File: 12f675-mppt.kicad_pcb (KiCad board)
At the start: 2 copper layers, 97.6 x 77.1 mm, 43 parts, among them IC1 PIC12F629-I/P, J1 S+, J2 S-, J3 O+, J4 O-, Q1 BUK9511-55A127, Q2 BUK9511-55A127, Q3 2N2222A, Q4 2N2222A, Q5 2N2907A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

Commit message: update PCB.
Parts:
- added R11: 10k, Resistors_THT:R_Axial_DIN0309_L9.0mm_D3.2mm_P12.70mm_Horizontal, F.Cu at (93.5, 85.3)
- moved C5 3.36 mm to (102.3, 74.4)
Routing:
- net /BootStrap: track 86.5 -> 97.0 mm
- net Net-(IC1-Pad7): track 8.67 -> 13.7 mm
- net /PV-Current: track 54.1 -> 58.7 mm
- net GNDPWR: track 290.1 -> 291.8 mm
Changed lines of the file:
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@@
     (thickness 1.6)
     (drawings 5)
-    (tracks 210)
+    (tracks 215)
     (zones 0)
-    (modules 43)
+    (modules 44)
     (nets 28)
   )
@@
   )
   (module Capacitors_THT:CP_Radial_D12.5mm_P5.00mm (layer F.Cu)
-    (at 99.02444 75.08748 270)
+    (at 102.32644 74.4474 270)
     (descr "CP, Radial series, Radial, pin pitch=5.00mm, , diameter=12.5mm, Electrolytic Capacitor")
     (tags "CP Radial series Radial pin pitch 5.00mm  diameter 12.5mm Electrolytic Capacitor")
@@
       (net 24 PRI_LO))
   )
+  (module Resistors_THT:R_Axial_DIN0309_L9.0mm_D3.2mm_P12.70mm_Horizontal (layer F.Cu)
+    (at 93.53804 85.33384 90)
+    (descr "Resistor, Axial_DIN0309 series, Axial, Horizontal, pin pitch=12.7mm, 0.5W = 1/2W, length*diameter=9*3.2mm^2, http://cdn-reichelt.de/documents/datenblatt/B400/1_4W%23YAG.pdf")
+    (tags "Resistor Axial_DIN0309 series Axial Horizontal pin pitch 12.7mm 0.5W = 1/2W length 9mm diameter 3.2mm")
+    (fp_text reference R11 (at 0.10668 2.82448 90) (layer F.SilkS)
+      (effects (font (size 1 1) (thickness 0.15)))
+    )
+    (fp_text value 10k (at 6.35 2.66 90) (layer F.Fab)
+      (effects (font (size 1 1) (thickness 0.15)))
+    )
+    (fp_line (start 13.75 -1.95) (end -1.05 -1.95) (layer F.CrtYd) (width 0.05))
+    (fp_line (start 13.75 1.95) (end 13.75 -1.95) (layer F.CrtYd) (width 0.05))
+    (fp_line (start -1.05 1.95) (end 13.75 1.95) (layer F.CrtYd) (width 0.05))
+    (fp_line (start -1.05 -1.95) (end -1.05 1.95) (layer F.CrtYd) (width 0.05))
+    (fp_line (start 11.72 0) (end 10.91 0) (layer F.SilkS) (width 0.12))
+    (fp_line (start 0.98 0) (end 1.79 0) (layer F.SilkS) (width 0.12))
+    (fp_line (start 10.91 -1.66) (end 1.79 -1.66) (layer F.SilkS) (width 0.12))
+    (fp_line (start 10.91 1.66) (end 10.91 -1.66) (layer F.SilkS) (width 0.12))
+    (fp_line (start 1.79 1.66) (end 10.91 1.66) (layer F.SilkS) (width 0.12))
+    (fp_line (start 1.79 -1.66) (end 1.79 1.66) (layer F.SilkS) (width 0.12))
+    (fp_line (start 12.7 0) (end 10.85 0) (layer F.Fab) (width 0.1))
+    (fp_line (start 0 0) (end 1.85 0) (layer F.Fab) (width 0.1))
+    (fp_line (start 10.85 -1.6) (end 1.85 -1.6) (layer F.Fab) (width 0.1))
+    (fp_line (start 10.85 1.6) (end 10.85 -1.6) (layer F.Fab) (width 0.1))
+    (fp_line (start 1.85 1.6) (end 10.85 1.6) (layer F.Fab) (width 0.1))
+    (fp_line (start 1.85 -1.6) (end 1.85 1.6) (layer F.Fab) (width 0.1))
+    (pad 2 thru_hole oval (at 12.7 0 90) (size 1.6 1.6) (drill 0.8) (layers *.Cu *.Mask)
+      (net 13 "Net-(IC1-Pad7)"))
+    (pad 1 thru_hole circle (at 0 0 90) (size 1.6 1.6) (drill 0.8) (layers *.Cu *.Mask)
+      (net 3 /BootStrap))
+    (model ${KISYS3DMOD}/Resistors_THT.3dshapes/R_Axial_DIN0309_L9.0mm_D3.2mm_P12.70mm_Horizontal.wrl
+      (at (xyz 0 0 0))
+      (scale (xyz 0.393701 0.393701 0.393701))
+      (rotate (xyz 0 0 0))
+    )
+  )
   (gr_text "25V 3A" (at 34.83356 57.84088 90) (layer F.SilkS)
     (effects (font (size 1.5 1.5) (thickness 0.3)))
@@
   (segment (start 83.99272 76.89088) (end 83.97748 76.87564) (width 1.5) (layer B.Cu) (net 3))
   (segment (start 88.49868 76.89088) (end 83.99272 76.89088) (width 1.5) (layer B.Cu) (net 3))
+  (segment (start 88.49868 80.29448) (end 93.53804 85.33384) (width 1.5) (layer F.Cu) (net 3))
+  (segment (start 88.49868 76.89088) (end 88.49868 80.29448) (width 1.5) (layer F.Cu) (net 3))
   (segment (start 102.72268 40.606728) (end 102.73284 40.596568) (width 2) (layer B.Cu) (net 4))
   (segment (start 102.72268 41.87952) (end 102.72268 40.606728) (width 2) (layer B.Cu) (net 4))
@@
   (segment (start 76.71308 76.87564) (end 83.91144 69.67728) (width 1.5) (layer F.Cu) (net 10))
   (segment (start 76.35748 76.87564) (end 76.71308 76.87564) (width 1.5) (layer F.Cu) (net 10))
-  (segment (start 96.32444 75.08748) (end 94.16036 72.9234) (width 1.5) (layer F.Cu) (net 10))
-  (segment (start 99.02444 75.08748) (end 96.32444 75.08748) (width 1.5) (layer F.Cu) (net 10))
-  (segment (start 86.61144 69.67728) (end 83.91144 69.67728) (width 1.5) (layer F.Cu) (net 10))
-  (segment (start 89.85756 72.9234) (end 86.61144 69.67728) (width 1.5) (layer F.Cu) (net 10))
-  (segment (start 94.16036 72.9234) (end 89.85756 72.9234) (width 1.5) (layer F.Cu) (net 10))
   (segment (start 76.35748 76.87564) (end 72.46112 76.87564) (width 1.5) (layer F.Cu) (net 10))
   (segment (start 58.2676 91.06916) (end 58.2676 93.28404) (width 1.5) (layer F.Cu) (net 10))
   (segment (start 72.46112 76.87564) (end 58.2676 91.06916) (width 1.5) (layer F.Cu) (net 10))
+  (segment (start 86.61144 69.67728) (end 93.28656 76.3524) (width 1.5) (layer F.Cu) (net 10))
+  (segment (start 83.91144 69.67728) (end 86.61144 69.67728) (width 1.5) (layer F.Cu) (net 10))
+  (segment (start 97.72144 76.3524) (end 93.28656 76.3524) (width 1.5) (layer F.Cu) (net 10))
+  (segment (start 99.62644 74.4474) (end 97.72144 76.3524) (width 1.5) (layer F.Cu) (net 10))
+  (segment (start 102.32644 74.4474) (end 99.62644 74.4474) (width 1.5) (layer F.Cu) (net 10))
   (segment (start 78.99144 64.59728) (end 79.11084 64.71668) (width 1.5) (layer B.Cu) (net 11))
   (segment (start 76.29144 64.59728) (end 78.99144 64.59728) (width 1.5) (layer B.Cu) (net 11))
@@
   (segment (start 86.69528 64.59728) (end 83.91144 64.59728) (width 1.5) (layer B.Cu) (net 13))
   (segment (start 90.86088 68.76288) (end 86.69528 64.59728) (width 1.5) (layer B.Cu) (net 13))
+  (segment (start 93.53804 71.44004) (end 90.86088 68.76288) (width 1.5) (layer B.Cu) (net 13))
+  (segment (start 93.53804 72.63384) (end 93.53804 71.44004) (width 1.5) (layer B.Cu) (net 13))
   (segment (start 50.78388 97.66032) (end 50.78388 104.16032) (width 2) (layer B.Cu) (net 14))
   (segment (start 50.73396 97.6104) (end 50.78388 97.66032) (width 1.5) (layer B.Cu) (net 14))
@@
   (segment (start 88.79332 99.66452) (end 93.5736 99.66452) (width 2) (layer B.Cu) (net 26))
   (segment (start 87.53348 98.40468) (end 88.79332 99.66452) (width 2) (layer B.Cu) (net 26))
-  (segment (start 99.02444 97.11368) (end 99.02444 80.08748) (width 2) (layer B.Cu) (net 26))
-  (segment (start 96.4736 99.66452) (end 99.02444 97.11368) (width 2) (layer B.Cu) (net 26))
-  (segment (start 93.5736 99.66452) (end 96.4736 99.66452) (width 2) (layer B.Cu) (net 26))
+  (segment (start 95.9736 99.66452) (end 98.21672 97.4214) (width 1.5) (layer B.Cu) (net 26))
+  (segment (start 93.5736 99.66452) (end 95.9736 99.66452) (width 1.5) (layer B.Cu) (net 26))
+  (segment (start 98.21672 83.55712) (end 102.32644 79.4474) (width 1.5) (layer B.Cu) (net 26))
+  (segment (start 98.21672 97.4214) (end 98.21672 83.55712) (width 1.5) (layer B.Cu) (net 26))
   (segment (start 40.7162 46.63948) (end 40.78224 46.70552) (width 3) (layer B.Cu) (net 27))
   (segment (start 40.7162 41.60012) (end 40.7162 46.63948) (width 3) (layer B.Cu) (net 27))

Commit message: Change circuit. Exchange GP0(Current Sensing) and GP2(PWM).
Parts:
- R1: value 4.7k -> 10k
- R15: value 10k -> 3.3k
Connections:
- IC1 pad 5: /PV-Current -> Net-(IC1-Pad5)
- IC1 pad 7: Net-(IC1-Pad7) -> /PV-Current
- R11 pad 2: Net-(IC1-Pad7) -> Net-(IC1-Pad5)
- R7 pad 2: Net-(IC1-Pad7) -> Net-(IC1-Pad5)
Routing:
- net Net-(IC1-Pad7): track 13.7 -> 0.00 mm
- net Net-(IC1-Pad5): track 0.00 -> 12.3 mm
- net /PV-Current: track 58.7 -> 69.0 mm

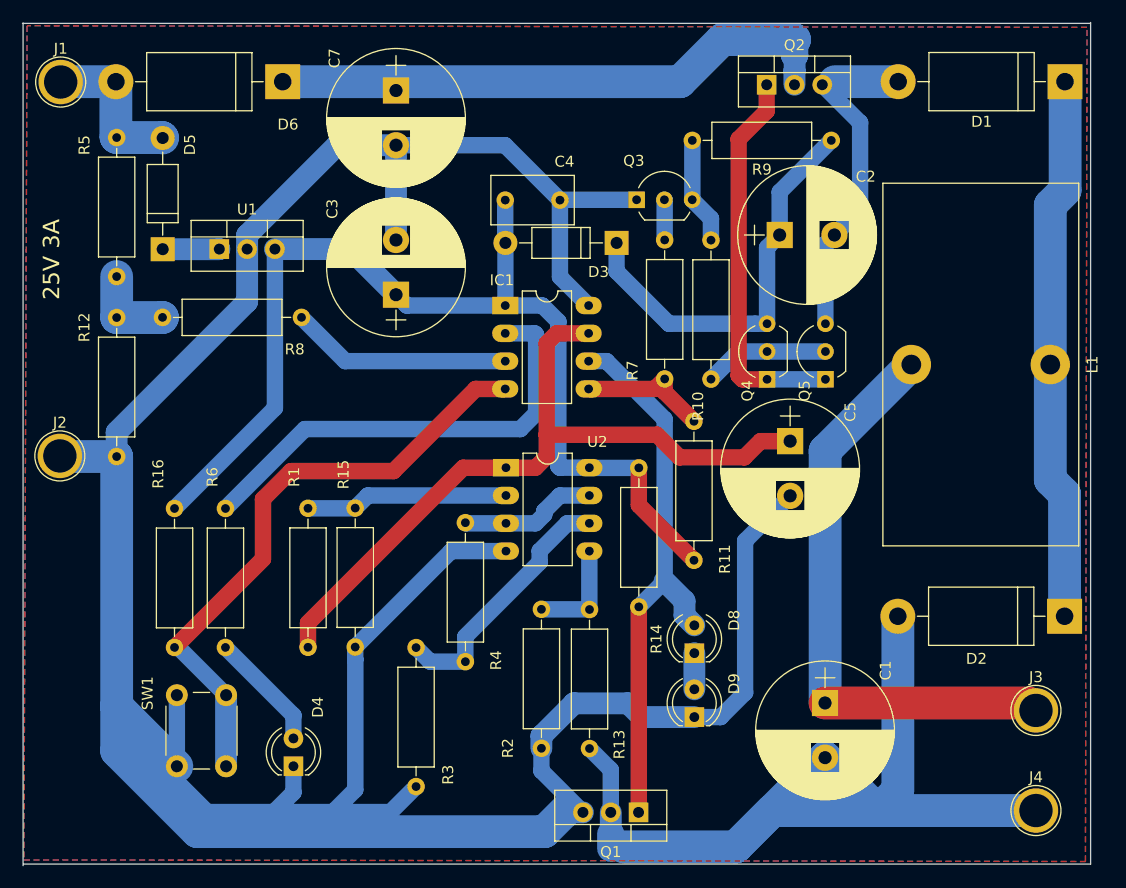
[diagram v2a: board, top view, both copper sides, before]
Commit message: Add FET protection zener diode.
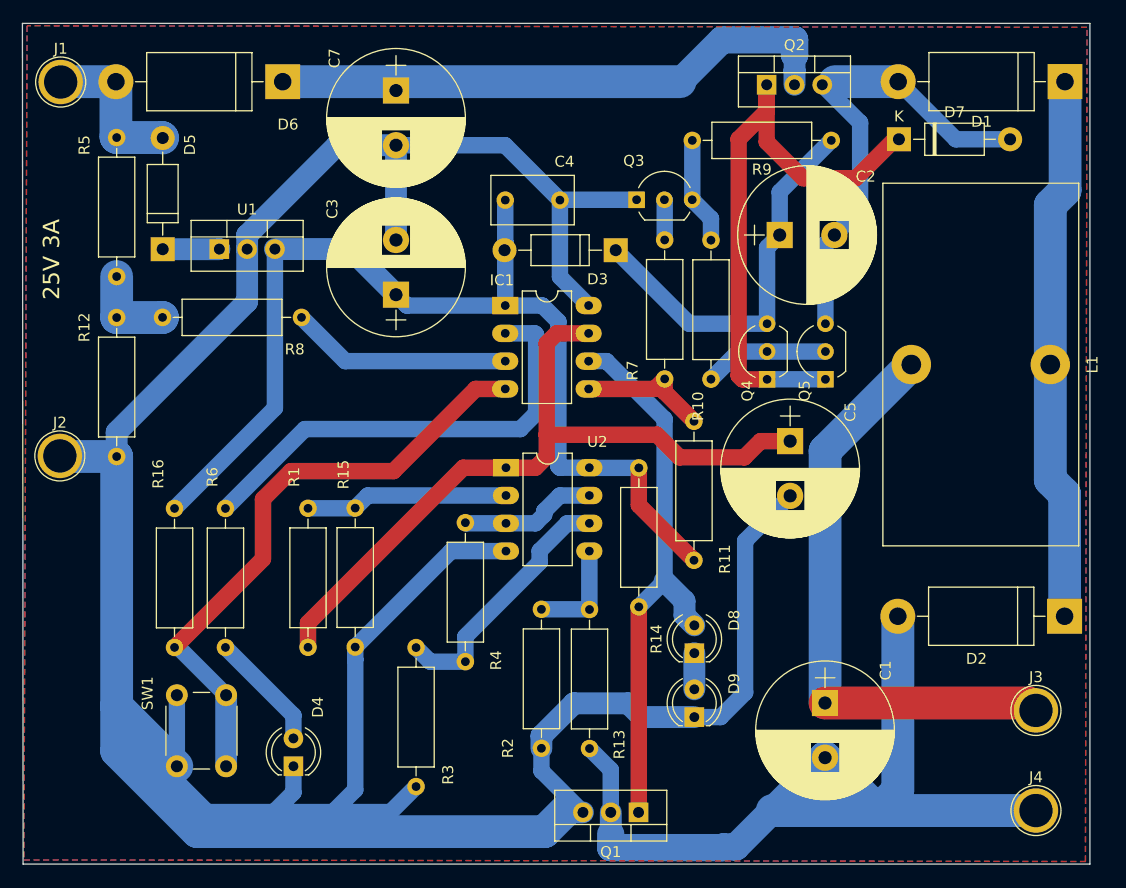
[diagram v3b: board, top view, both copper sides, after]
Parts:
- added D7: 1N4733A 5.1V, Diode_THT:D_DO-41_SOD81_P10.16mm_Horizontal, F.Cu at (112.3, 46.9)
- moved D3 0.67 mm to (86.4, 57.0)
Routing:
- net Net-(D7-Pad1): track 35.7 -> 55.9 mm
- net Net-(C7-Pad1): track 52.6 -> 66.1 mm
- net Net-(C2-Pad2): track 30.4 -> 42.8 mm
- net PRI_LO: track 94.0 -> 88.8 mm
- net Net-(C2-Pad1): track 37.5 -> 35.8 mm
- net /BootStrap: track 97.0 -> 96.3 mm
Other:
- board size 97.6 x 77.1 mm -> 97.6 x 76.8 mm

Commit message: R9 -> 2.2k
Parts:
- R9: value 10k -> 2.2k

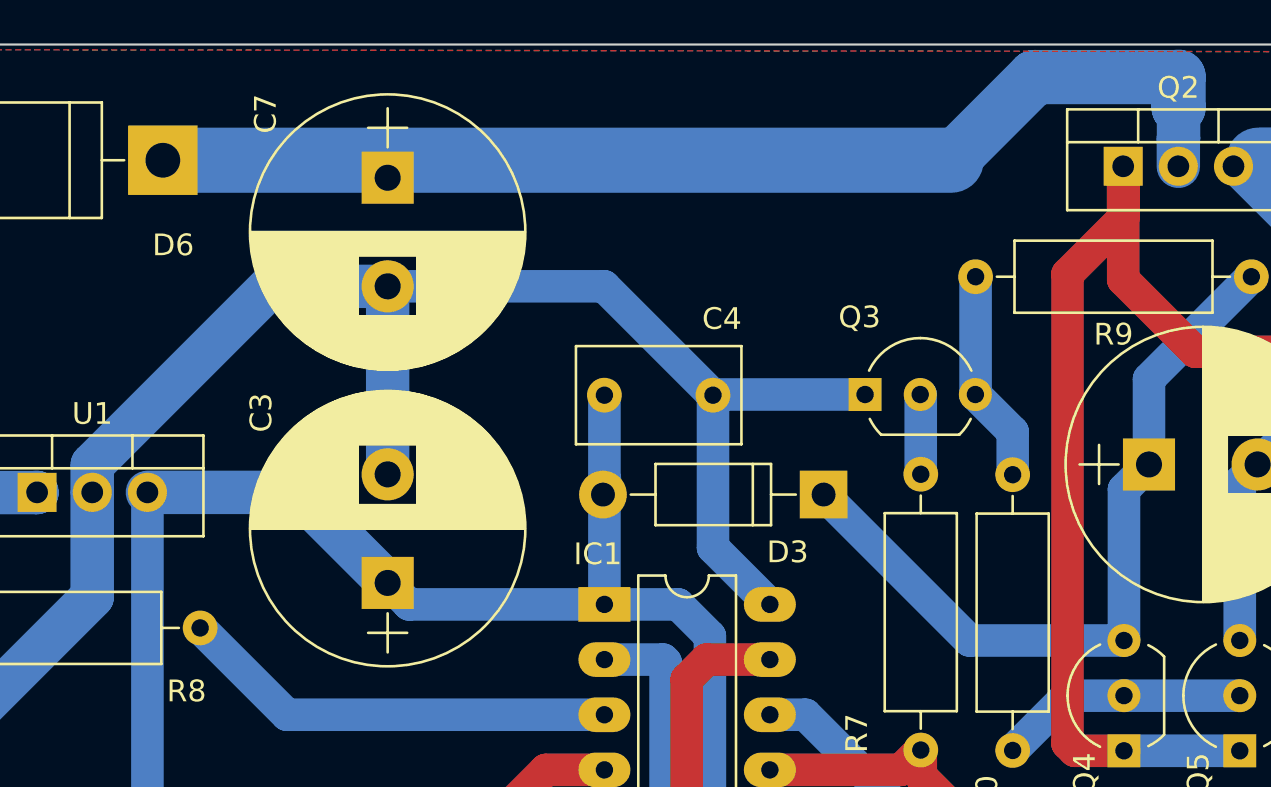
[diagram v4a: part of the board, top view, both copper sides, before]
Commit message: Fix FET Bootstrap problem.
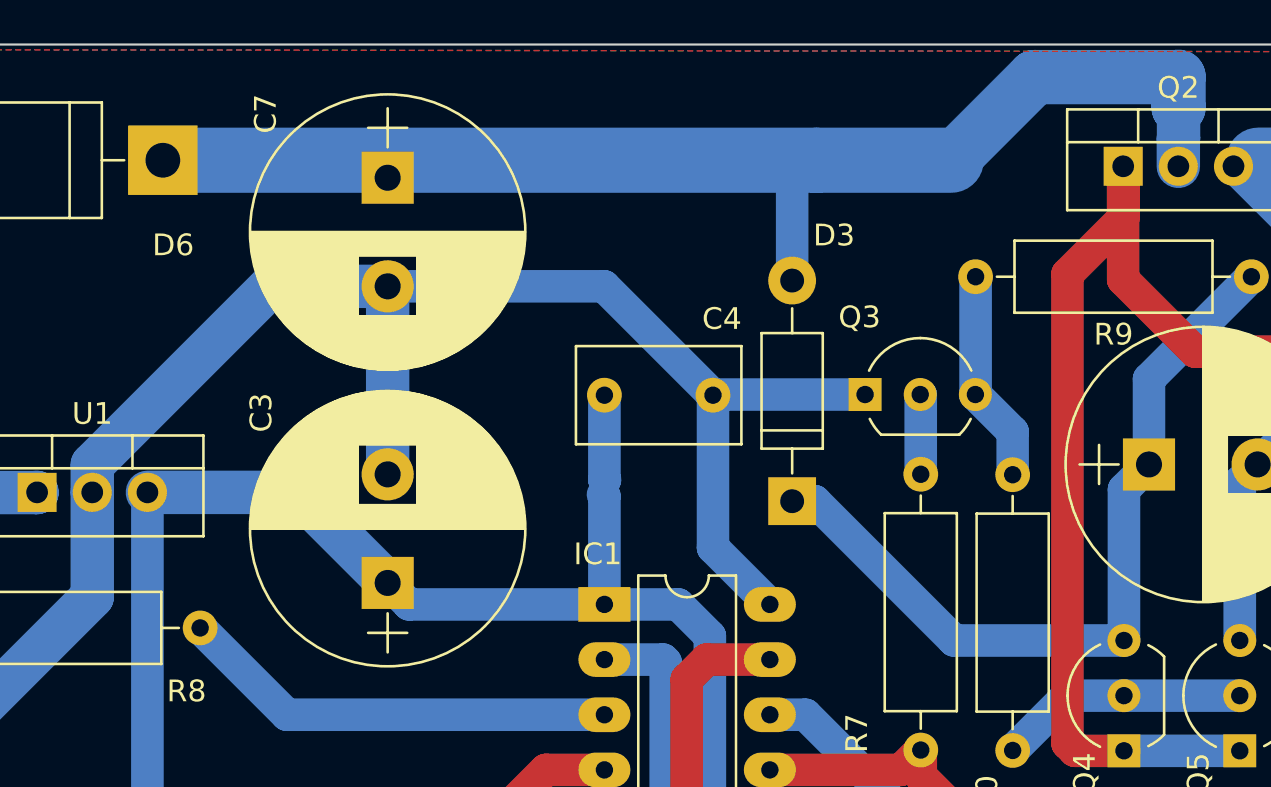
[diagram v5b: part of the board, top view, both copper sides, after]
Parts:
- C2: value 10u 50v -> 4.7u 50v
- moved D3 1.48 mm to (84.9, 57.3), turned to 90 degrees
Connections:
- C2 pad 1: Net-(C2-Pad1) -> /BootStrap
- C3 pad 1: /BootStrap -> Net-(C3-Pad1)
- C4 pad 1: /BootStrap -> Net-(C3-Pad1)
- D3 pad 1: Net-(C2-Pad1) -> /BootStrap
- D3 pad 2: /BootStrap -> Net-(C7-Pad1)
- IC1 pad 1: /BootStrap -> Net-(C3-Pad1)
- Q4 pad 3: Net-(C2-Pad1) -> /BootStrap
- R11 pad 1: /BootStrap -> Net-(C3-Pad1)
- R14 pad 1: /BootStrap -> Net-(C3-Pad1)
- R16 pad 2: /BootStrap -> Net-(C3-Pad1)
- R9 pad 1: Net-(C2-Pad1) -> /BootStrap
- U1 pad 3: /BootStrap -> Net-(C3-Pad1)
- U2 pad 8: /BootStrap -> Net-(C3-Pad1)
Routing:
- net Net-(C3-Pad1): track 0.00 -> 96.3 mm
- net /BootStrap: track 96.3 -> 37.1 mm
- net Net-(C2-Pad1): track 35.8 -> 0.00 mm
- net Net-(C7-Pad1): track 66.1 -> 72.1 mm

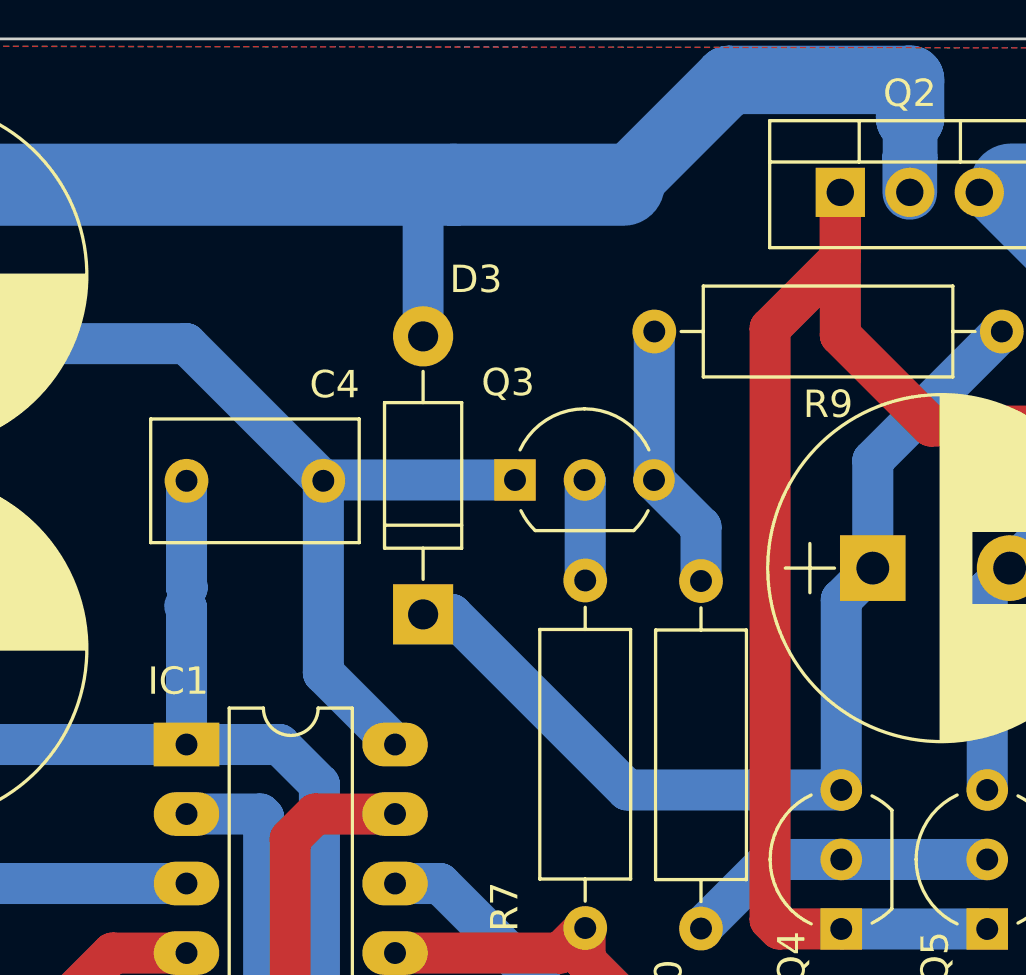
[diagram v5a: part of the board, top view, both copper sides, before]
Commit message: Revert and Change diode.
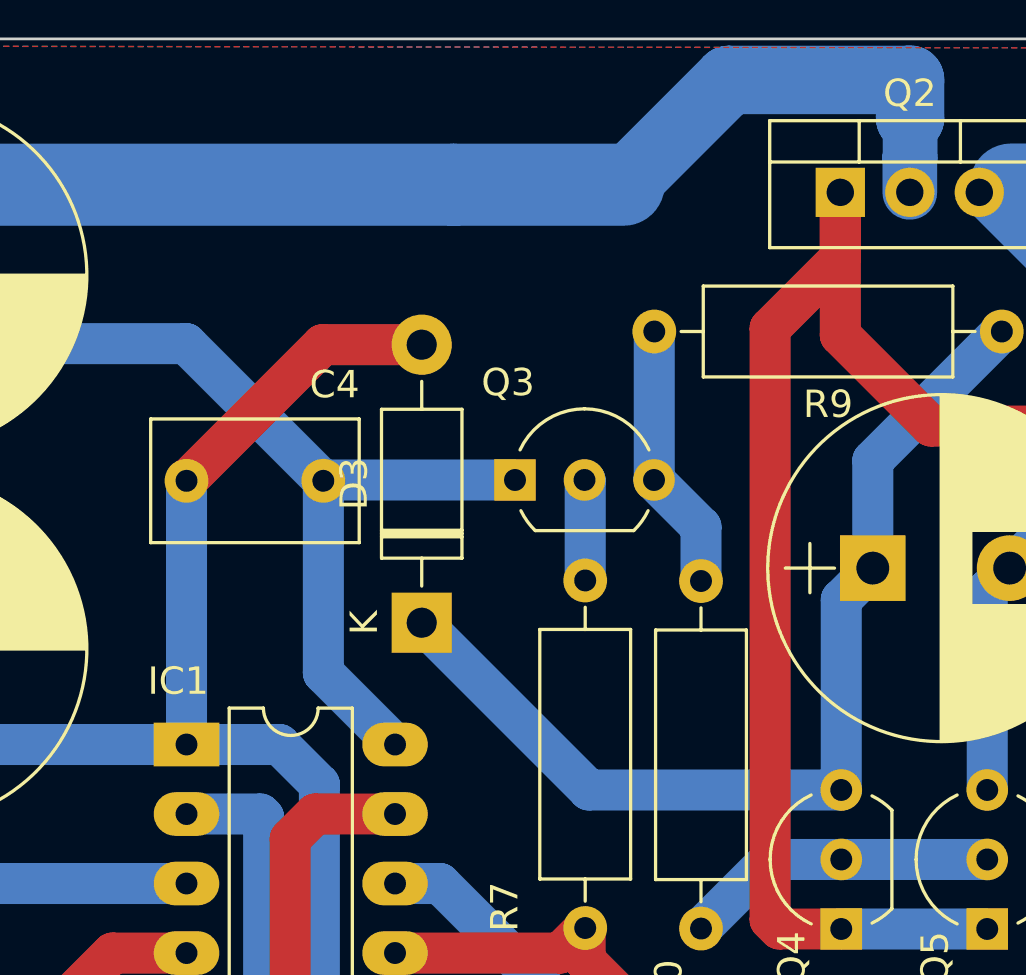
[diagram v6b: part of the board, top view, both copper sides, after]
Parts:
- D3: value 1N4148 -> 1N5819; footprint Diodes_THT:D_DO-41_SOD81_P10.16mm_Horizontal -> Diode_THT:D_DO-41_SOD81_P10.16mm_Horizontal
- moved D3 0.31 mm to (84.9, 57.6)
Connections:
- D3 pad 2: Net-(C7-Pad1) -> Net-(C3-Pad1)
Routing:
- net Net-(C3-Pad1): track 96.3 -> 107.6 mm
- net Net-(C7-Pad1): track 72.1 -> 66.1 mm
